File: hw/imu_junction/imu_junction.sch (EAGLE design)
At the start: 50 parts, among them J1 JST-PH3SMT_VERT, J2 JST-PH3SMT_VERT, J3 JST-PH3SMT_VERT, J4 JST-PH3SMT_VERT, J5 JST-XH4SMT_RA, U1 STM32F4R_64PIN, U2 BMI088LGA16, U3 TPS62177WSON10, U4 SN65HVD75SOIC8, U5 SN65HVD75SOIC8, U6 SN65HVD75SOIC8, X1 8.0MHz

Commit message: More work on IMU junction board
Everything roughly placed on the board
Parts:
- added C16, C17, C18: 0.1uF 50V, mfpassives:CAPACITOR_NP_0402
- added U$5: MOUNTM2, controller:MOUNTM2
- U4, U5, U6: value SN65HVD75SOIC8 -> MAX13431E; device imu_junction:SN65HVD75SOIC8 -> controller:MAX13431E; MF (none) -> Maxim; MPN (none) -> MAX13431EETB+T; POPULATE (none) -> 1
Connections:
- new net DIR1: U1.PC8/TIM3_3/TIM8_3/UART6_CK, U4.DE, U4.RE/
- new net DIR2: U1.PA1/TIM2_2/TIM5_2/UART4_RX, U5.DE, U5.RE/
- new net DIR3: U1.PC12/I2C2_SDA/SPI3_MOSI/I2S3_SD/UART3_CK/UART5_TX, U6.DE, U6.RE/
- new net IMU_CS1: U1.PB6/TIM4_1/I2C1_SCL/UART1_TX, U2.CSB1
- new net IMU_CS2: U1.PB7/TIM4_2/I2C1_SDA/UART1_RX, U2.CSB2
- new net IMU_MISO: U1.PB4/NJTRST/TIM3_1/I2C3_SDA/SPI1_MISO/SPI3_MISO, U2.SDO1, U2.SDO2
- new net IMU_MOSI: U1.PB5/TIM3_2/SPI1_MOSI/I2S1_SD/SPI3_MOSI/I2S3_SD, U2.SDI
- new net IMU_SCK: U1.PB3/SWO/TIM2_2/I2C2_SDA/SPI1_SCK/I2S1_CK/SPI3_SCK/I2S3_CK, U2.SCK
- new net RX1: U1.PC7/TIM3_2/TIM8_2/SPI2_SCK/I2S2_CK/I2S3_MCK/UART6_RX, U4.RO
- new net RX2: U1.PA3/TIM2_4/TIM5_4/TIM9_2/UART2_RX, U5.RO
- new net RX3: U1.PC11/SPI3_MISO/UART3_RX/UART4_RX, U6.RO
- new net TX1: U1.PC6/TIM3_1/TIM8_1/I2S2_MCK/UART6_RX, U4.DI
- new net TX2: U1.PA2/TIM2_3/TIM5_3/TIM9_1/UART2_TX, U5.DI
- new net TX3: U1.PC10/SPI3_SCK/I2S3_CK/UART3_TX/UART4_TX, U6.DI
- net +3V3: now also C16.P$1, C17.P$1, C18.P$1, U4.VCC, U4.VL, U5.VCC, U5.VL, U6.VCC, U6.VL
- net GND: now also C16.P$2, C17.P$2, C18.P$2
- net N$2: now also U1.PA9/TIM1_2/SPI2_SCK/I2S3_CK/UART1_TX/USB_VBUS; no longer U1.PB6/TIM4_1/I2C1_SCL/UART1_TX
- net N$3: now also U1.PA10/TIM1_3/USART1_RX; no longer U1.PB7/TIM4_2/I2C1_SDA/UART1_RX
- net N$9: no longer U4.A
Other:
- moved on the sheet: DRX, DTX

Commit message: Progress on imu-junction
Parts placed and power routed
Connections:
- new net IMU_ACC_INT: U1.PC14, U2.INT1
- new net IMU_GYRO_INT: U1.PC13, U2.INT3
- net DIR1: now also U1.PA1/TIM2_2/TIM5_2/UART4_RX; no longer U1.PC8/TIM3_3/TIM8_3/UART6_CK
- net DIR2: now also U1.PC8/TIM3_3/TIM8_3/UART6_CK; no longer U1.PA1/TIM2_2/TIM5_2/UART4_RX
- net GND: now also U2.PS; no longer C13.P$2, C14.P$2, C15.P$2, J1.3, J2.3, J3.3, J4.3, J5.1, U3.FB
- net N$9: now also U4.A
- net RX1: now also U1.PA3/TIM2_4/TIM5_4/TIM9_2/UART2_RX; no longer U1.PC7/TIM3_2/TIM8_2/SPI2_SCK/I2S2_CK/I2S3_MCK/UART6_RX
- net RX2: now also U1.PC7/TIM3_2/TIM8_2/SPI2_SCK/I2S2_CK/I2S3_MCK/UART6_RX; no longer U1.PA3/TIM2_4/TIM5_4/TIM9_2/UART2_RX
- net TX1: now also U1.PA2/TIM2_3/TIM5_3/TIM9_1/UART2_TX; no longer U1.PC6/TIM3_1/TIM8_1/I2S2_MCK/UART6_RX
- net TX2: now also U1.PC6/TIM3_1/TIM8_1/I2S2_MCK/UART6_RX; no longer U1.PA2/TIM2_3/TIM5_3/TIM9_1/UART2_TX
- net V-: now also C13.P$2, C14.P$2, C15.P$2, J1.3, J2.3, J3.3, J4.3, J5.1, U3.FB, U3.NC
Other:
- moved on the sheet: SH4

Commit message: imu_junction: Align all parts and rough align silk
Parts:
- added D1: MF-LED-0603-RED, mfleds:LED_SINGLE-0603-RED
- added D2: MF-LED-0603-GREEN, mfleds:LED_SINGLE-0603-GREEN
- added R2, R3: 220, mfpassives:RESISTOR_0402
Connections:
- net N$4 renamed D2_P
- net N$5 renamed D2_N
- net N$8 renamed D1_N
- net N$9 renamed D1_P
- net SLAVE_RX renamed D3_P
- net SLAVE_TX renamed D3_N
- new net N$5: D1.ANODE, R2.P$1
- new net N$8: D2.ANODE, R3.P$1
- new net STATUS1: D1.CATHODE, U1.PB13/TIM1_1N/SPI2_SCK/I2S2_CK
- new net STATUS2: D2.CATHODE, U1.PB12
- net +3V3: now also R2.P$2, R3.P$2
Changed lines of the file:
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@@
 </part>
 <part name="GND8" library="supply1" deviceset="GND" device=""/>
+<part name="D1" library="mfleds" deviceset="LED_SINGLE" device="-0603-RED" value="MF-LED-0603-RED"/>
+<part name="D2" library="mfleds" deviceset="LED_SINGLE" device="-0603-GREEN" value="MF-LED-0603-GREEN"/>
+<part name="R2" library="mfpassives" deviceset="RESISTOR" device="_0402" value="220">
+<attribute name="HOUSEPART" value="1"/>
+<attribute name="MPN" value="MF-RES-0402-220"/>
+</part>
+<part name="R3" library="mfpassives" deviceset="RESISTOR" device="_0402" value="220">
+<attribute name="HOUSEPART" value="1"/>
+<attribute name="MPN" value="MF-RES-0402-220"/>
+</part>
+<part name="+3V7" library="supply1" deviceset="+3V3" device=""/>
 </parts>
 <sheets>
@@
 </instance>
 <instance part="GND8" gate="1" x="68.58" y="-215.9"/>
+<instance part="D1" gate="G$1" x="185.42" y="-86.36" rot="R270"/>
+<instance part="D2" gate="G$1" x="200.66" y="-86.36" rot="R270"/>
+<instance part="R2" gate="G$1" x="185.42" y="-76.2" rot="R180">
+<attribute name="MPN" x="185.42" y="-76.2" size="1.778" layer="96" rot="R180" display="off"/>
+</instance>
+<instance part="R3" gate="G$1" x="200.66" y="-76.2" rot="R180">
+<attribute name="MPN" x="200.66" y="-76.2" size="1.778" layer="96" rot="R180" display="off"/>
+</instance>
+<instance part="+3V7" gate="G$1" x="195.58" y="-66.04"/>
 </instances>
 <busses>
@@
 <junction x="22.86" y="-375.92"/>
 </segment>
+<segment>
+<pinref part="R2" gate="G$1" pin="P$2"/>
+<wire x1="185.42" y1="-71.12" x2="185.42" y2="-68.58" width="0.1524" layer="91"/>
+<pinref part="+3V7" gate="G$1" pin="+3V3"/>
+<wire x1="185.42" y1="-68.58" x2="195.58" y2="-68.58" width="0.1524" layer="91"/>
+<pinref part="R3" gate="G$1" pin="P$2"/>
+<wire x1="195.58" y1="-68.58" x2="200.66" y2="-68.58" width="0.1524" layer="91"/>
+<wire x1="200.66" y1="-68.58" x2="200.66" y2="-71.12" width="0.1524" layer="91"/>
+<junction x="195.58" y="-68.58"/>
+</segment>
 </net>
 <net name="GND" class="0">
@@
 </segment>
 </net>
-<net name="N$4" class="0">
+<net name="D2_P" class="0">
 <segment>
 <pinref part="J3" gate="A" pin="1"/>
@@
 <junction x="104.14" y="-424.18"/>
 <pinref part="U5" gate="G$1" pin="A"/>
-</segment>
-</net>
-<net name="N$5" class="0">
+<label x="81.28" y="-424.18" size="1.778" layer="95"/>
+</segment>
+</net>
+<net name="D2_N" class="0">
 <segment>
 <wire x1="66.04" y1="-429.26" x2="68.58" y2="-429.26" width="0.1524" layer="91"/>
@@
 <pinref part="U5" gate="G$1" pin="B"/>
 <wire x1="66.04" y1="-431.8" x2="66.04" y2="-429.26" width="0.1524" layer="91"/>
-</segment>
-</net>
-<net name="N$8" class="0">
+<label x="81.28" y="-426.72" size="1.778" layer="95"/>
+</segment>
+</net>
+<net name="D1_N" class="0">
 <segment>
 <wire x1="66.04" y1="-381" x2="71.12" y2="-381" width="0.1524" layer="91"/>
@@
 <pinref part="U4" gate="G$1" pin="B"/>
 <wire x1="66.04" y1="-383.54" x2="66.04" y2="-381" width="0.1524" layer="91"/>
-</segment>
-</net>
-<net name="N$9" class="0">
+<label x="78.74" y="-378.46" size="1.778" layer="95"/>
+</segment>
+</net>
+<net name="D1_P" class="0">
 <segment>
 <pinref part="J1" gate="A" pin="1"/>
@@
 <junction x="104.14" y="-375.92"/>
 <pinref part="U4" gate="G$1" pin="A"/>
-</segment>
-</net>
-<net name="SLAVE_TX" class="0">
+<label x="78.74" y="-375.92" size="1.778" layer="95"/>
+</segment>
+</net>
+<net name="D3_N" class="0">
 <segment>
 <pinref part="J5" gate="G$1" pin="2"/>
@@
 <pinref part="U6" gate="G$1" pin="B"/>
 <wire x1="66.04" y1="-490.22" x2="66.04" y2="-487.68" width="0.1524" layer="91"/>
-</segment>
-</net>
-<net name="SLAVE_RX" class="0">
+<label x="88.9" y="-485.14" size="1.778" layer="95"/>
+</segment>
+</net>
+<net name="D3_P" class="0">
 <segment>
 <pinref part="J5" gate="G$1" pin="3"/>
 <wire x1="66.04" y1="-482.6" x2="137.16" y2="-482.6" width="0.1524" layer="91"/>
 <pinref part="U6" gate="G$1" pin="A"/>
+<label x="88.9" y="-482.6" size="1.778" layer="95"/>
 </segment>
 </net>
@@
 </segment>
 </net>
+<net name="N$5" class="0">
+<segment>
+<pinref part="R2" gate="G$1" pin="P$1"/>
+<pinref part="D1" gate="G$1" pin="ANODE"/>
+<wire x1="185.42" y1="-81.28" x2="185.42" y2="-83.82" width="0.1524" layer="91"/>
+</segment>
+</net>
+<net name="N$8" class="0">
+<segment>
+<pinref part="R3" gate="G$1" pin="P$1"/>
+<pinref part="D2" gate="G$1" pin="ANODE"/>
+<wire x1="200.66" y1="-81.28" x2="200.66" y2="-83.82" width="0.1524" layer="91"/>
+</segment>
+</net>
+<net name="STATUS2" class="0">
+<segment>
+<pinref part="D2" gate="G$1" pin="CATHODE"/>
+<wire x1="200.66" y1="-88.9" x2="200.66" y2="-101.6" width="0.1524" layer="91"/>
+<label x="200.66" y="-99.06" size="1.778" layer="95"/>
+</segment>
+<segment>
+<pinref part="U1" gate="G$1" pin="PB12"/>
+<wire x1="5.08" y1="-27.94" x2="-12.7" y2="-27.94" width="0.1524" layer="91"/>
+<label x="-12.7" y="-27.94" size="1.778" layer="95"/>
+</segment>
+</net>
+<net name="STATUS1" class="0">
+<segment>
+<pinref part="D1" gate="G$1" pin="CATHODE"/>
+<wire x1="185.42" y1="-88.9" x2="185.42" y2="-101.6" width="0.1524" layer="91"/>
+<label x="185.42" y="-99.06" size="1.778" layer="95"/>
+</segment>
+<segment>
+<pinref part="U1" gate="G$1" pin="PB13/TIM1_1N/SPI2_SCK/I2S2_CK"/>
+<wire x1="5.08" y1="-30.48" x2="-12.7" y2="-30.48" width="0.1524" layer="91"/>
+<label x="-12.7" y="-30.48" size="1.778" layer="95"/>
+</segment>
+</net>

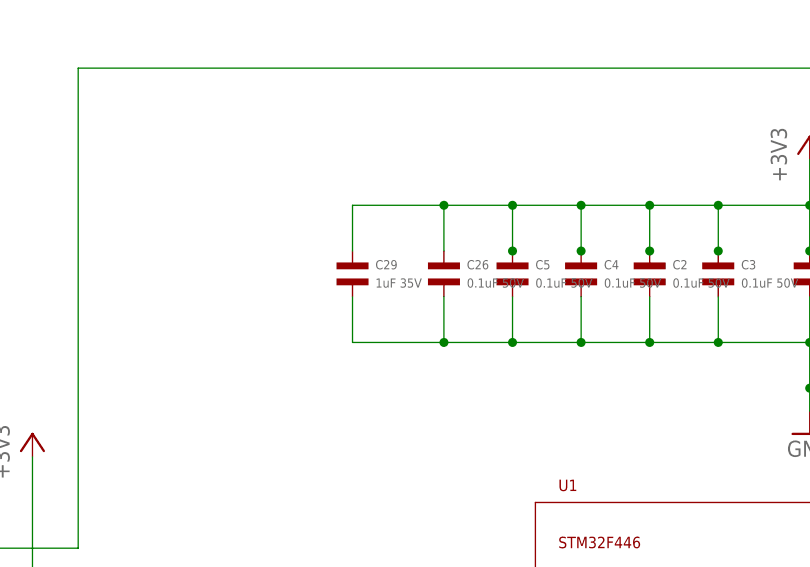
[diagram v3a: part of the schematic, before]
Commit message: imu_junction: Finalize BOM
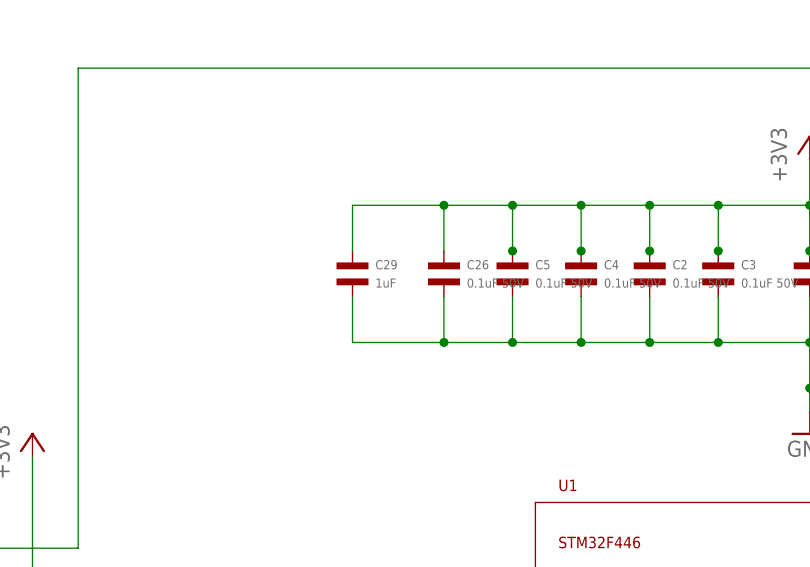
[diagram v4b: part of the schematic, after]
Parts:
- C1, C7: MPN (none) -> CL10A475KA8NQNC
- C10, C11, C15, C16, C17, C18, C2, C26, C3, C4, C5, C6: MF TDK -> Walsin; MPN (none) -> 0402B104K500CT
- C13: MPN MF-CAP-1206-10uF -> MF-CAP-1206-10uF
- C29: value 1uF 35V -> 1uF; HOUSEPART (none) -> YES; MF Samsung Electro-Mechanics -> (none); MPN (none) -> MF-CAP-0402-1uF
- C8, C9: device mfpassives:CAPACITOR_NP_0402 -> mfpassives:CAPACITOR_NP_0603; HOUSEPART (none) -> 1; MF Samsung Electro-Mechanics -> (none); MPN (none) -> MF-CAP-0603-10pF
- DGND, DRX, DTX: POPULATE (none) -> 0
- J5: AMFPN S4B-XH-SM4-TB(LF)(SN) -> (none); MPN (none) -> S4B-XH-SM4-TB(LF)(SN); POPULATE (none) -> 1
- U2: POPULATE (none) -> 1
- U3: MF (none) -> TI; MPN (none) -> TPS62177DQCR; POPULATE (none) -> 1
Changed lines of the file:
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@@
 </part>
 <part name="C2" library="mfpassives" deviceset="CAPACITOR_NP" device="_0402" value="0.1uF 50V">
-<attribute name="MF" value="TDK"/>
+<attribute name="MF" value="Walsin"/>
+<attribute name="MPN" value="0402B104K500CT"/>
 </part>
 <part name="C6" library="mfpassives" deviceset="CAPACITOR_NP" device="_0402" value="0.1uF 50V">
-<attribute name="MF" value="TDK"/>
+<attribute name="MF" value="Walsin"/>
+<attribute name="MPN" value="0402B104K500CT"/>
 </part>
 <part name="C4" library="mfpassives" deviceset="CAPACITOR_NP" device="_0402" value="0.1uF 50V">
-<attribute name="MF" value="TDK"/>
+<attribute name="MF" value="Walsin"/>
+<attribute name="MPN" value="0402B104K500CT"/>
 </part>
 <part name="C5" library="mfpassives" deviceset="CAPACITOR_NP" device="_0402" value="0.1uF 50V">
-<attribute name="MF" value="TDK"/>
+<attribute name="MF" value="Walsin"/>
+<attribute name="MPN" value="0402B104K500CT"/>
 </part>
 <part name="C3" library="mfpassives" deviceset="CAPACITOR_NP" device="_0402" value="0.1uF 50V">
-<attribute name="MF" value="TDK"/>
+<attribute name="MF" value="Walsin"/>
+<attribute name="MPN" value="0402B104K500CT"/>
 </part>
 <part name="C1" library="mfpassives" deviceset="CAPACITOR_NP" device="_0603" value="4.7uF">
 <attribute name="MF" value="Samsung Electro-Mechanics"/>
+<attribute name="MPN" value="CL10A475KA8NQNC"/>
 </part>
 <part name="GND1" library="supply1" deviceset="GND" device=""/>
@@
 <part name="C7" library="mfpassives" deviceset="CAPACITOR_NP" device="_0603" value="4.7uF">
 <attribute name="MF" value="Samsung Electro-Mechanics"/>
+<attribute name="MPN" value="CL10A475KA8NQNC"/>
 </part>
 <part name="X1" library="controller" deviceset="CRYSTAL" device="ABM3B" value="8.0MHz">
@@
 </part>
 <part name="GND17" library="supply1" deviceset="GND" device=""/>
-<part name="C8" library="mfpassives" deviceset="CAPACITOR_NP" device="_0402" value="10pF">
-<attribute name="MF" value="Samsung Electro-Mechanics"/>
-</part>
-<part name="C9" library="mfpassives" deviceset="CAPACITOR_NP" device="_0402" value="10pF">
-<attribute name="MF" value="Samsung Electro-Mechanics"/>
+<part name="C8" library="mfpassives" deviceset="CAPACITOR_NP" device="_0603" value="10pF">
+<attribute name="HOUSEPART" value="1"/>
+<attribute name="MF" value=""/>
+<attribute name="MPN" value="MF-CAP-0603-10pF"/>
+</part>
+<part name="C9" library="mfpassives" deviceset="CAPACITOR_NP" device="_0603" value="10pF">
+<attribute name="HOUSEPART" value="1"/>
+<attribute name="MF" value=""/>
+<attribute name="MPN" value="MF-CAP-0603-10pF"/>
 </part>
 <part name="GND6" library="supply1" deviceset="GND" device=""/>
@@
 </part>
 <part name="C26" library="mfpassives" deviceset="CAPACITOR_NP" device="_0402" value="0.1uF 50V">
-<attribute name="MF" value="TDK"/>
-</part>
-<part name="C29" library="mfpassives" deviceset="CAPACITOR_NP" device="_0402" value="1uF 35V">
-<attribute name="MF" value="Samsung Electro-Mechanics"/>
-</part>
-<part name="DGND" library="controller" deviceset="PAD" device="24AWG_PAD"/>
+<attribute name="MF" value="Walsin"/>
+<attribute name="MPN" value="0402B104K500CT"/>
+</part>
+<part name="C29" library="mfpassives" deviceset="CAPACITOR_NP" device="_0402" value="1uF">
+<attribute name="HOUSEPART" value="YES"/>
+<attribute name="MF" value=""/>
+<attribute name="MPN" value="MF-CAP-0402-1uF"/>
+</part>
+<part name="DGND" library="controller" deviceset="PAD" device="24AWG_PAD">
+<attribute name="POPULATE" value="0"/>
+</part>
 <part name="GND2" library="supply1" deviceset="GND" device=""/>
 <part name="C10" library="mfpassives" deviceset="CAPACITOR_NP" device="_0402" value="0.1uF 50V">
-<attribute name="MF" value="TDK"/>
+<attribute name="MF" value="Walsin"/>
+<attribute name="MPN" value="0402B104K500CT"/>
 </part>
 <part name="C11" library="mfpassives" deviceset="CAPACITOR_NP" device="_0402" value="0.1uF 50V">
-<attribute name="MF" value="TDK"/>
+<attribute name="MF" value="Walsin"/>
+<attribute name="MPN" value="0402B104K500CT"/>
 </part>
 <part name="U2" library="imu_junction" deviceset="BMI088" device="LGA16">
 <attribute name="MF" value="Bosch Sensortec"/>
 <attribute name="MPN" value="BMI088"/>
+<attribute name="POPULATE" value="1"/>
 </part>
 <part name="+3V1" library="supply1" deviceset="+3V3" device=""/>
-<part name="U3" library="imu_junction" deviceset="TPS62177" device="WSON10"/>
+<part name="U3" library="imu_junction" deviceset="TPS62177" device="WSON10">
+<attribute name="MF" value="TI"/>
+<attribute name="MPN" value="TPS62177DQCR"/>
+<attribute name="POPULATE" value="1"/>
+</part>
 <part name="L1" library="mfpassives" deviceset="INDUCTOR" device="_1210" value="10uH">
 <attribute name="HOUSEPART" value="1"/>
@@
 <part name="C13" library="mfpassives" deviceset="CAPACITOR_NP" device="_1206" value="10uF">
 <attribute name="HOUSEPART" value="1"/>
-<attribute name="MPN" value="
-MF-CAP-1206-10uF"/>
+<attribute name="MPN" value="MF-CAP-1206-10uF"/>
 </part>
 <part name="C14" library="mfpassives" deviceset="CAPACITOR_NP" device="_1206" value="10uF">
@@
 </part>
 <part name="C15" library="mfpassives" deviceset="CAPACITOR_NP" device="_0402" value="0.1uF 50V">
-<attribute name="MF" value="TDK"/>
+<attribute name="MF" value="Walsin"/>
+<attribute name="MPN" value="0402B104K500CT"/>
 </part>
 <part name="J1" library="controller" deviceset="JST-PH3" device="SMT_VERT" value="JST-PH3SMT_VERT">
@@
 </part>
 <part name="J5" library="gimbal" deviceset="JST-XH4" device="SMT_RA">
-<attribute name="AMFPN" value="S4B-XH-SM4-TB(LF)(SN)"/>
 <attribute name="DPN" value="455-2262-1-ND"/>
+<attribute name="MPN" value="S4B-XH-SM4-TB(LF)(SN)"/>
+<attribute name="POPULATE" value="1"/>
 </part>
 <part name="SH4" library="shorts" deviceset="SHORT" device="BIG" value="SHORTBIG">
@@
 <part name="+3V6" library="supply1" deviceset="+3V3" device=""/>
 <part name="C17" library="mfpassives" deviceset="CAPACITOR_NP" device="_0402" value="0.1uF 50V">
-<attribute name="MF" value="TDK"/>
+<attribute name="MF" value="Walsin"/>
+<attribute name="MPN" value="0402B104K500CT"/>
 </part>
 <part name="C18" library="mfpassives" deviceset="CAPACITOR_NP" device="_0402" value="0.1uF 50V">
-<attribute name="MF" value="TDK"/>
+<attribute name="MF" value="Walsin"/>
+<attribute name="MPN" value="0402B104K500CT"/>
 </part>
 <part name="C16" library="mfpassives" deviceset="CAPACITOR_NP" device="_0402" value="0.1uF 50V">
-<attribute name="MF" value="TDK"/>
-</part>
-<part name="DTX" library="controller" deviceset="PAD" device="24AWG_PAD"/>
-<part name="DRX" library="controller" deviceset="PAD" device="24AWG_PAD"/>
+<attribute name="MF" value="Walsin"/>
+<attribute name="MPN" value="0402B104K500CT"/>
+</part>
+<part name="DTX" library="controller" deviceset="PAD" device="24AWG_PAD">
+<attribute name="POPULATE" value="0"/>
+</part>
+<part name="DRX" library="controller" deviceset="PAD" device="24AWG_PAD">
+<attribute name="POPULATE" value="0"/>
+</part>
 <part name="U$5" library="controller" deviceset="MOUNT" device="M2" value="MOUNTM2">
 <attribute name="POPULATE" value="0"/>
@@
 <attribute name="MF" x="-7.62" y="86.36" size="1.778" layer="96" display="off"/>
 </instance>
-<instance part="DGND" gate="G$1" x="106.68" y="-68.58"/>
+<instance part="DGND" gate="G$1" x="106.68" y="-68.58">
+<attribute name="POPULATE" x="106.68" y="-68.58" size="1.778" layer="96" display="off"/>
+</instance>
 <instance part="GND2" gate="1" x="119.38" y="-218.44"/>
 <instance part="C10" gate="G$1" x="134.62" y="-205.74">
@@
 <attribute name="MPN" x="86.36" y="-195.58" size="1.778" layer="96" display="off"/>
 <attribute name="MF" x="86.36" y="-195.58" size="1.778" layer="96" display="off"/>
+<attribute name="POPULATE" x="86.36" y="-195.58" size="1.778" layer="96" display="off"/>
 </instance>
 <instance part="+3V1" gate="G$1" x="119.38" y="-190.5"/>
-<instance part="U3" gate="G$1" x="88.9" y="-292.1"/>
+<instance part="U3" gate="G$1" x="88.9" y="-292.1">
+<attribute name="MPN" x="88.9" y="-292.1" size="1.778" layer="96" display="off"/>
+<attribute name="MF" x="88.9" y="-292.1" size="1.778" layer="96" display="off"/>
+<attribute name="POPULATE" x="88.9" y="-292.1" size="1.778" layer="96" display="off"/>
+</instance>
 <instance part="L1" gate="G$1" x="116.84" y="-281.94"/>
 <instance part="+3V2" gate="G$1" x="132.08" y="-274.32"/>
@@
 <instance part="J5" gate="G$1" x="144.78" y="-482.6" rot="R180">
 <attribute name="DPN" x="144.78" y="-482.6" size="1.778" layer="96" rot="R180" display="off"/>
-<attribute name="AMFPN" x="144.78" y="-482.6" size="1.778" layer="96" rot="R180" display="off"/>
+<attribute name="MPN" x="144.78" y="-482.6" size="1.778" layer="96" rot="R180" display="off"/>
+<attribute name="POPULATE" x="144.78" y="-482.6" size="1.778" layer="96" rot="R180" display="off"/>
 </instance>
 <instance part="SH4" gate="G$1" x="88.9" y="-325.12">
@@
 <attribute name="MF" x="17.78" y="-398.78" size="1.778" layer="96" display="off"/>
 </instance>
-<instance part="DTX" gate="G$1" x="-81.28" y="20.32" rot="R180"/>
-<instance part="DRX" gate="G$1" x="-91.44" y="17.78" rot="R180"/>
+<instance part="DTX" gate="G$1" x="-81.28" y="20.32" rot="R180">
+<attribute name="POPULATE" x="-81.28" y="20.32" size="1.778" layer="96" rot="R180" display="off"/>
+</instance>
+<instance part="DRX" gate="G$1" x="-91.44" y="17.78" rot="R180">
+<attribute name="POPULATE" x="-91.44" y="17.78" size="1.778" layer="96" rot="R180" display="off"/>
+</instance>
 <instance part="U$5" gate="G$1" x="50.8" y="124.46">
 <attribute name="POPULATE" x="50.8" y="124.46" size="1.778" layer="96" display="off"/>
